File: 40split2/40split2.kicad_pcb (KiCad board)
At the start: 2 copper layers, 22 parts

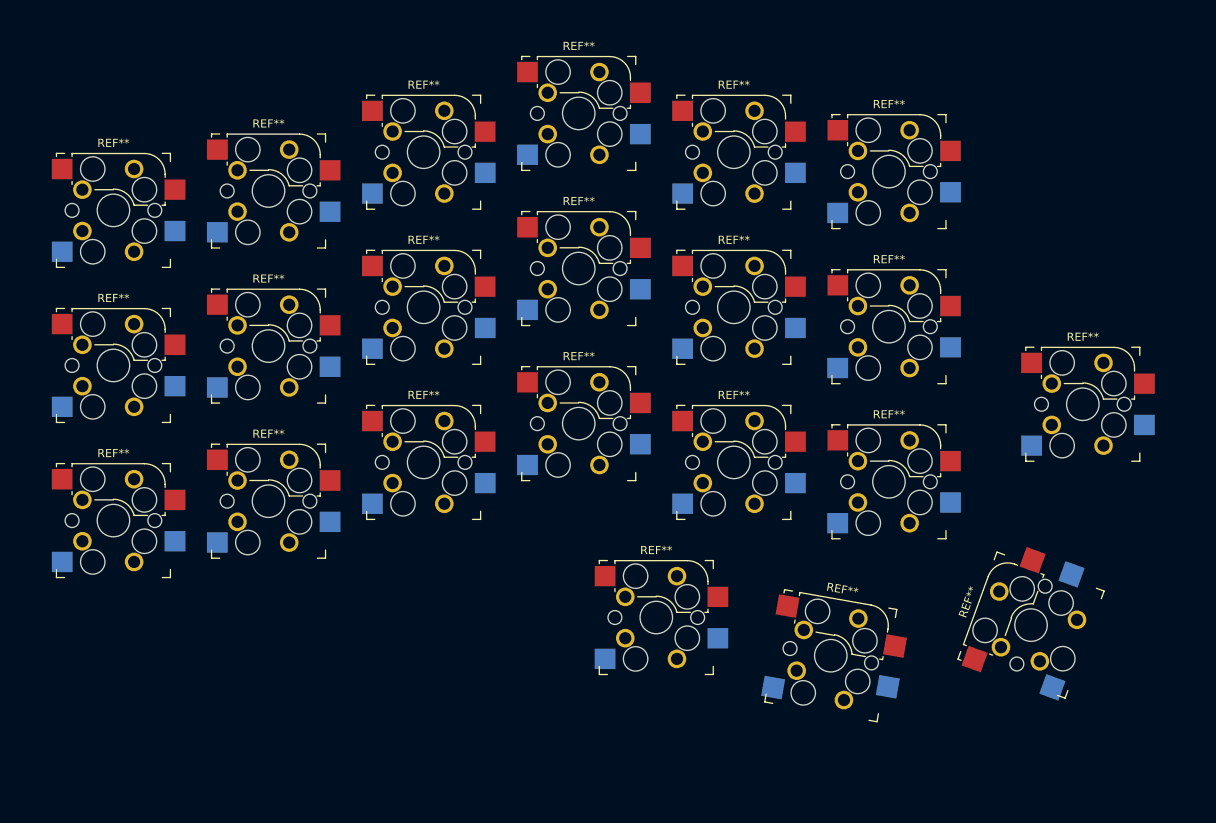
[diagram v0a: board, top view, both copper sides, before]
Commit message: further work to PCB: Add diode cluster and TRRS
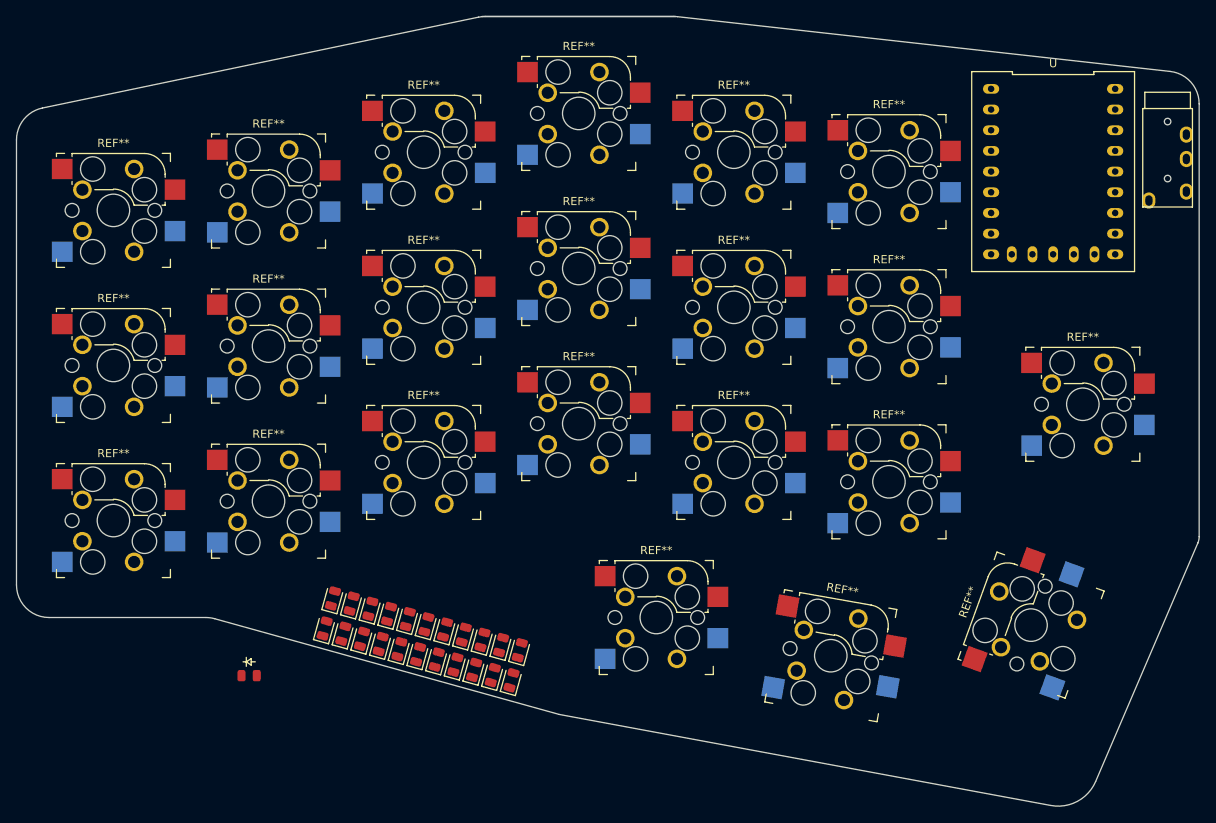
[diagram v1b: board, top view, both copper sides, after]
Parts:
- added REF**: D_0805_2012Metric, SMD Diodes:D_0805_2012Metric, F.Cu at (121.9, 134.3)
- added REF**: D_0805_2012Metric, SMD Diodes:D_0805_2012Metric, F.Cu at (131.1, 136.9)
- added REF**: D_0805_2012Metric, SMD Diodes:D_0805_2012Metric, F.Cu at (132.1, 133.2)
- added REF**: D_0805_2012Metric, SMD Diodes:D_0805_2012Metric, F.Cu at (118.4, 129.4)
- added REF**: D_0805_2012Metric, SMD Diodes:D_0805_2012Metric, F.Cu at (125.2, 131.3)
- added REF**: D_0805_2012Metric, SMD Diodes:D_0805_2012Metric, F.Cu at (124.2, 134.9)
- added REF**: D_0805_2012Metric, SMD Diodes:D_0805_2012Metric, F.Cu at (129.8, 132.5)
- added REF**: D_0805_2012Metric, SMD Diodes:D_0805_2012Metric, F.Cu at (117.3, 133.0)
- added REF**: D_0805_2012Metric, SMD Diodes:D_0805_2012Metric, F.Cu at (133.4, 137.5)
- added REF**: D_0805_2012Metric, SMD Diodes:D_0805_2012Metric, F.Cu at (128.8, 136.2)
- added REF**: D_0805_2012Metric, SMD Diodes:D_0805_2012Metric, F.Cu at (111.5, 127.4)
- added REF**: D_0805_2012Metric, SMD Diodes:D_0805_2012Metric, F.Cu at (113.8, 128.1)
- added REF**: D_0805_2012Metric, SMD Diodes:D_0805_2012Metric, F.Cu at (120.7, 130.0)
- added REF**: D_0805_2012Metric, SMD Diodes:D_0805_2012Metric, F.Cu at (126.5, 135.6)
- added REF**: D_0805_2012Metric, SMD Diodes:D_0805_2012Metric, F.Cu at (123.0, 130.6)
- added REF**: TRRS_PJ-320A, Scotto_lib:TRRS_PJ-320A, F.Cu at (214.0, 67.3)
- added REF**: LED_0805, Scotto_lib:LED_0805, F.Cu at (101.2, 136.9)
- added REF**: D_0805_2012Metric, SMD Diodes:D_0805_2012Metric, F.Cu at (134.4, 133.8)
- added REF**: D_0805_2012Metric, SMD Diodes:D_0805_2012Metric, F.Cu at (112.8, 131.8)
- added REF**: D_0805_2012Metric, SMD Diodes:D_0805_2012Metric, F.Cu at (115.0, 132.4)
- added REF**: D_0805_2012Metric, SMD Diodes:D_0805_2012Metric, F.Cu at (116.1, 128.7)
- added REF**: D_0805_2012Metric, SMD Diodes:D_0805_2012Metric, F.Cu at (110.5, 131.1)
- added REF**: D_0805_2012Metric, SMD Diodes:D_0805_2012Metric, F.Cu at (119.6, 133.7)
- added REF**: D_0805_2012Metric, SMD Diodes:D_0805_2012Metric, F.Cu at (127.5, 131.9)
- added U: RP2040-Zero, rp2040-zero:RP2040-Zero, F.Cu at (199.9, 75.0)
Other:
- board outline added: 145.3 x 97 mm
